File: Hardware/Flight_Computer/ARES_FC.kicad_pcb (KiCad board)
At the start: 2 copper layers, 57.2 x 57.2 mm, 67 parts, among them J1 SWD, J2 TYPE-C-31-M-12, J3 FC_M/P, J4 5V, J5 GND, J6 FC_RF, J7 Conn_01x04_Pin, J8 Conn_01x04_Pin, U1 STM32F401CCU6, U2 AMS1117-3.3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

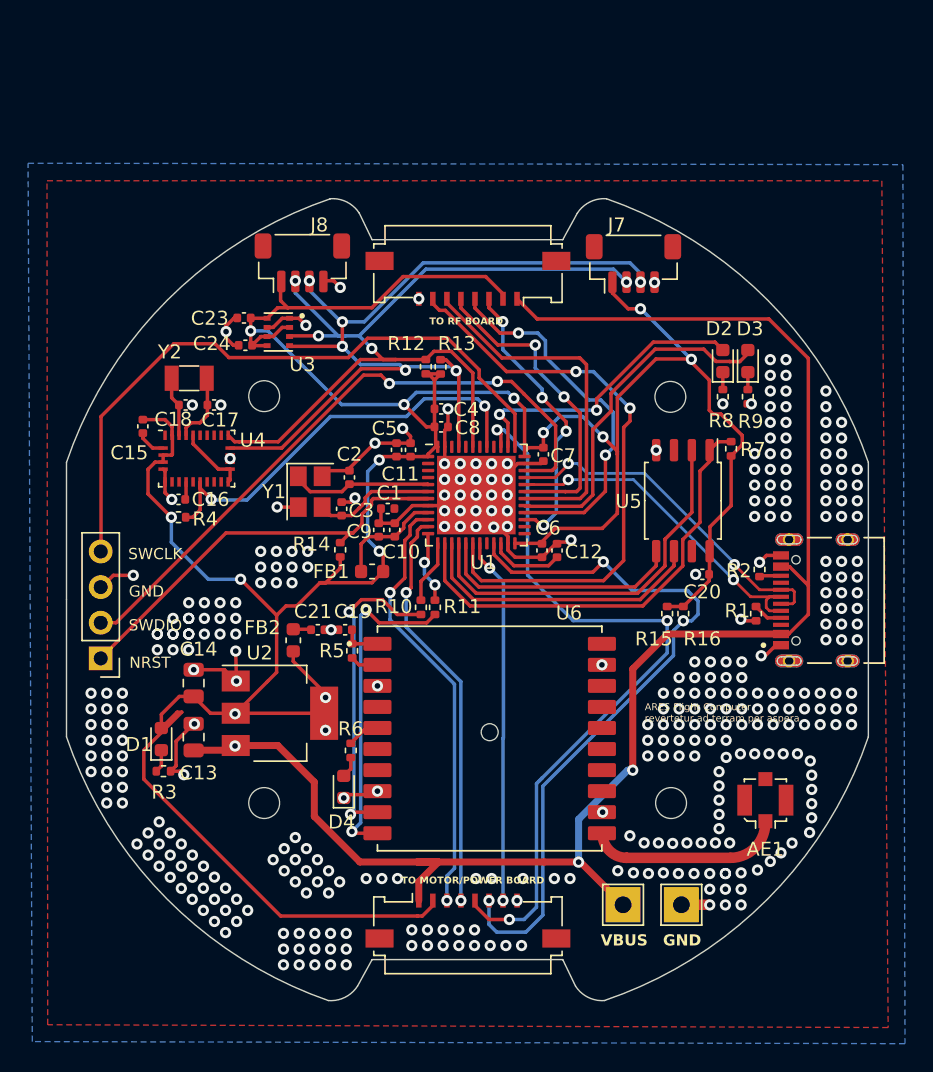
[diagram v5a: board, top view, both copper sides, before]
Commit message: aesthetic edits (silkscreen, etc.)
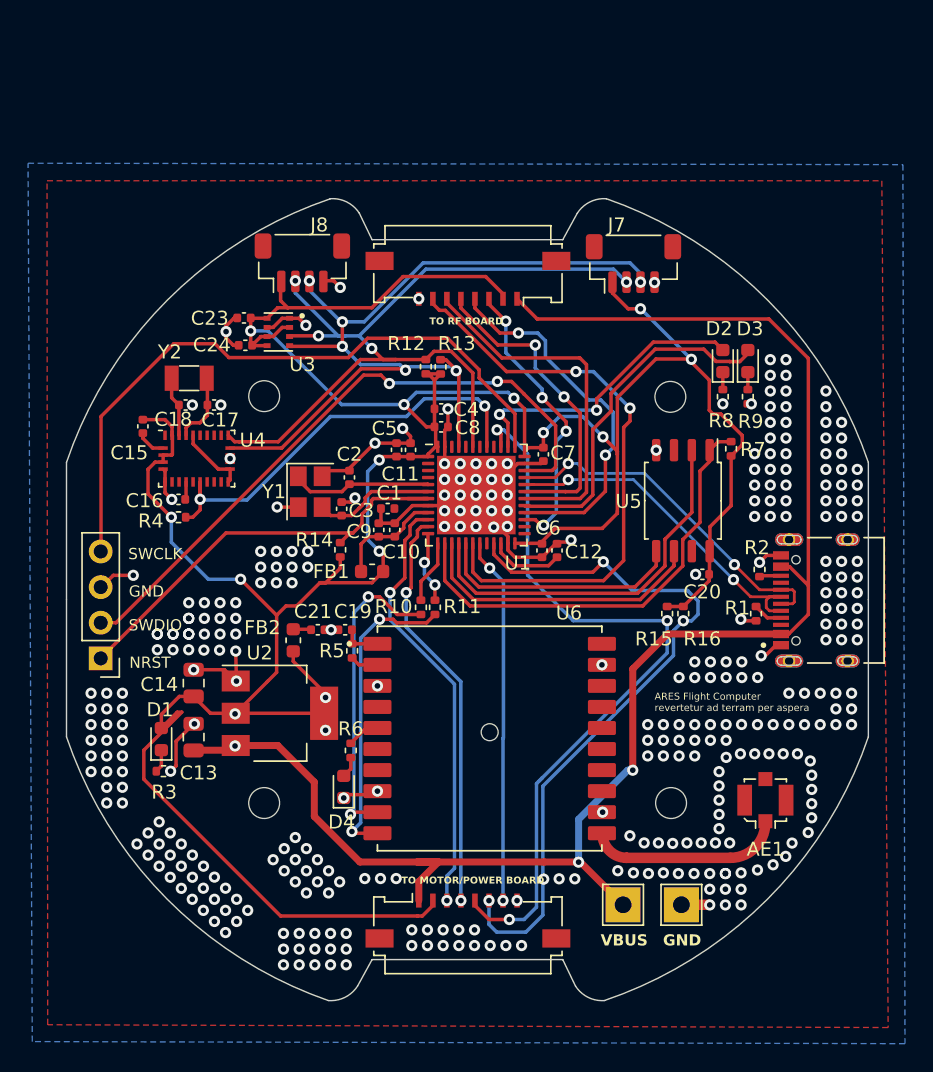
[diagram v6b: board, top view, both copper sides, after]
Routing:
- net Net-(U6-RX): track 23.6 -> 22.1 mm
- net GND: track 82.1 -> 81.0 mm, vias 362 -> 343

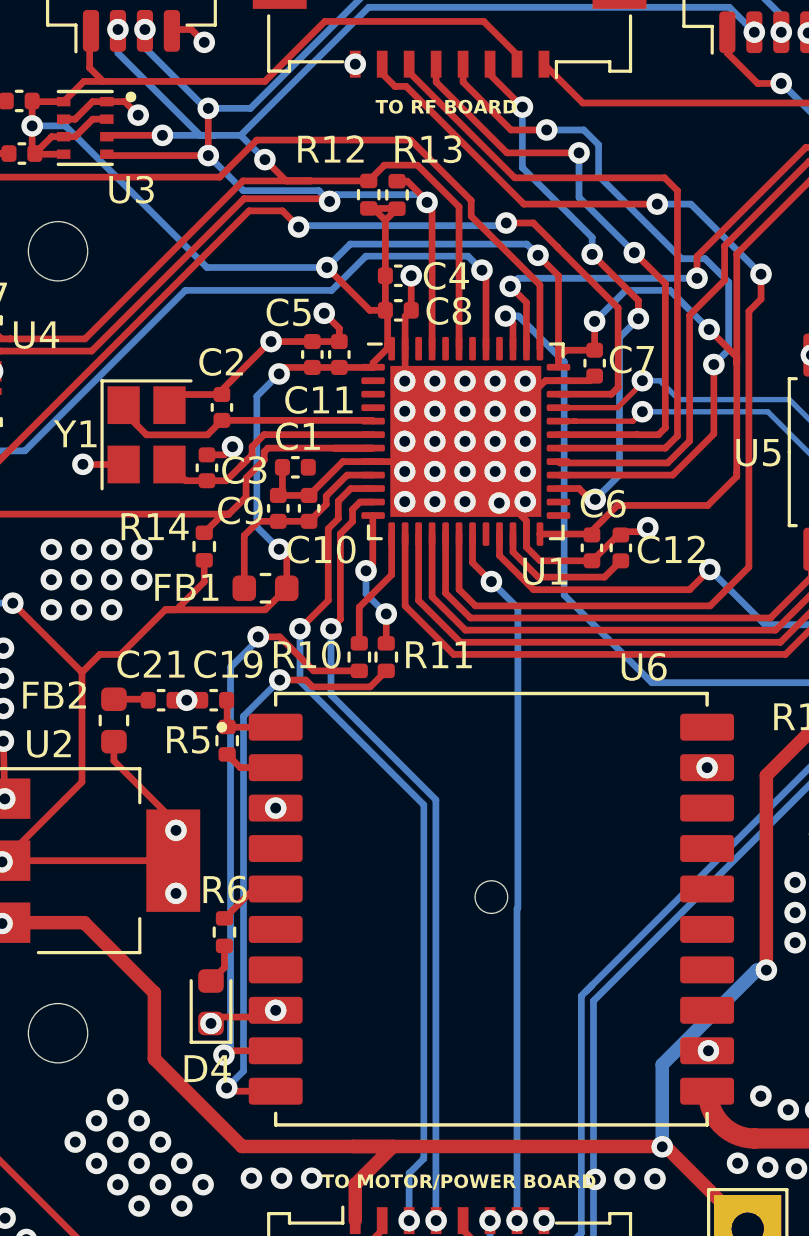
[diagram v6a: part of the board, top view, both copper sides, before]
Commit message: connected GPS_NRST to STM32
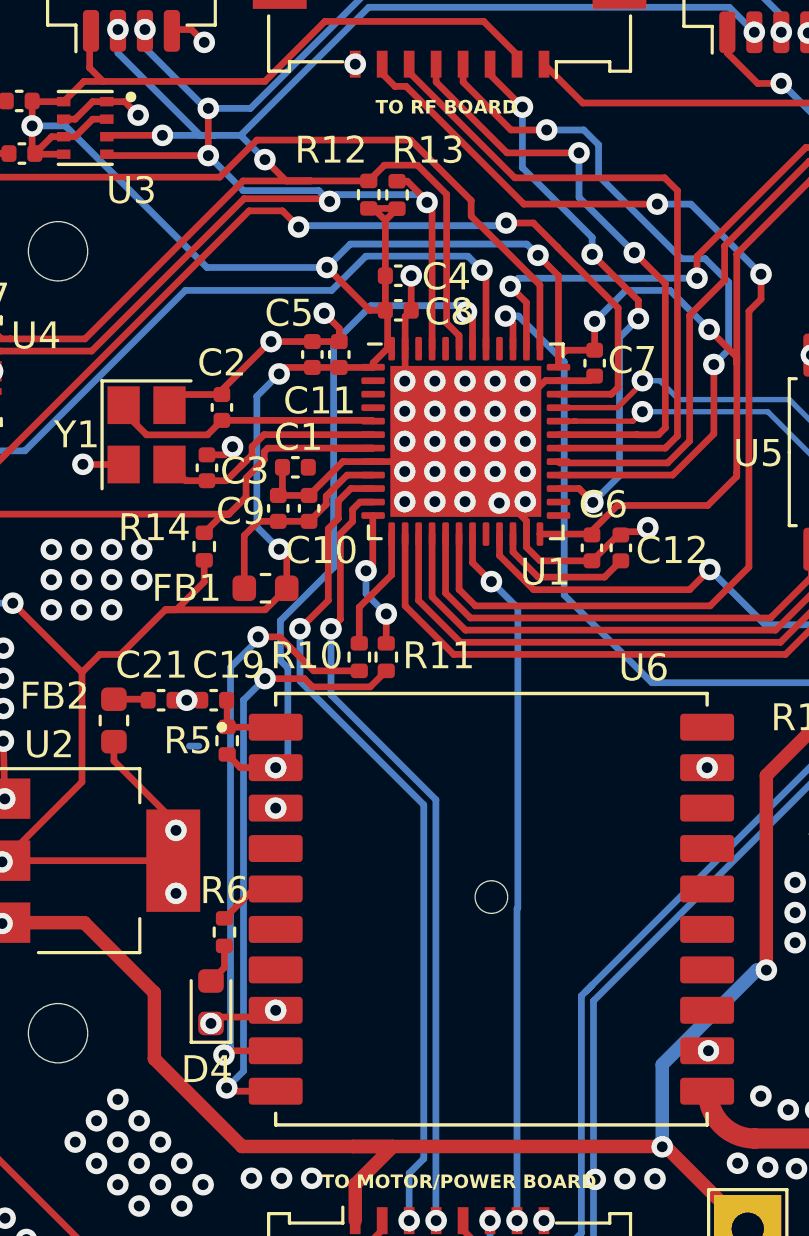
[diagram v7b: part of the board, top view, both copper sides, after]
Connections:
- R5 pad 2: /NRESET -> /GPS_NRST
- U1 pad 42: unconnected-(U1-PB6-Pad42) -> /GPS_NRST
- U6 pad 2: /NRESET -> /GPS_NRST
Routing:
- net /GPS_NRST: track 0.00 -> 26.3 mm, vias 0 -> 2
- net /NRESET: track 2.00 -> 0.00 mm
